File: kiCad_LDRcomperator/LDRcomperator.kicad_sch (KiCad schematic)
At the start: 9 parts, among them J1 Screw_Terminal_01x02

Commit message: updated the LDRComperator kicad drawing
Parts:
- removed Output1: Conn_01x01_MountingPin, Connector_PinSocket_2.54mm:PinSocket_1x01_P2.54mm_Vertical, symbol Connector_Generic_MountingPin:Conn_01x01_MountingPin
- added J2, J3: Conn_01x02_MountingPin, Connector_PinSocket_2.54mm:PinSocket_1x02_P2.54mm_Vertical, symbol Connector_Generic_MountingPin:Conn_01x02_MountingPin
- added LED2: LED, LED_THT:LED_D1.8mm_W3.3mm_H2.4mm, symbol Device:LED
- added R5: 65 ohm, Resistor_THT:R_Axial_DIN0204_L3.6mm_D1.6mm_P7.62mm_Horizontal, symbol Device:R
- added R6: LDR03, TerminalBlock_Phoenix:TerminalBlock_Phoenix_MKDS-1,5-2_1x02_P5.00mm_Horizontal, symbol Sensor_Optical:LDR03
- added R7: 2,2k ohm, Resistor_THT:R_Axial_DIN0204_L3.6mm_D1.6mm_P7.62mm_Horizontal, symbol Device:R
- J1, R2: footprint Connector_PinSocket_2.54mm:PinSocket_1x02_P2.54mm_Vertical -> TerminalBlock_Phoenix:TerminalBlock_Phoenix_MKDS-1,5-2_1x02_P5.00mm_Horizontal
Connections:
- net +3V3: now also R6.1
- net GND: now also LED2.1 (K), R7.2
- net at Op-amp1.1, R4.1: now also J2.1 (Pin_1), J2.2 (Pin_2)
- net at Op-amp1.3 (+), Potentiometer1.2, R1.2: now also Op-amp1.5 (+)
- new net: LED2.2 (A), R5.2
- new net: Op-amp1.6 (-), R6.2, R7.1
- new net: J3.1 (Pin_1), J3.2 (Pin_2), Op-amp1.7, R5.1
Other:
- moved on the sheet: J1, LED1, Potentiometer1, R1, R2, R3, R4

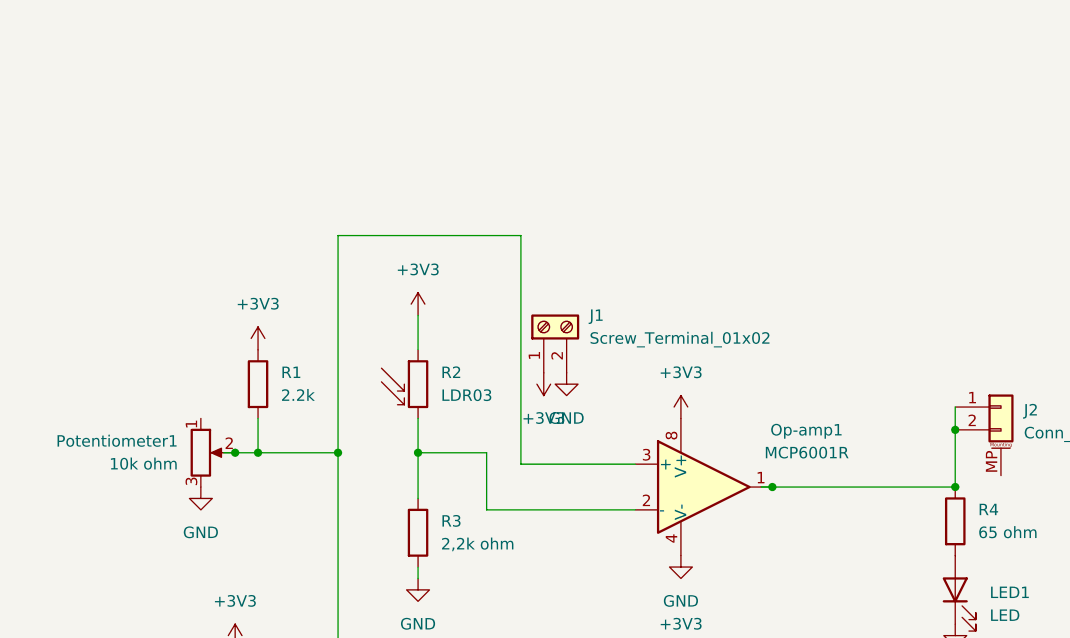
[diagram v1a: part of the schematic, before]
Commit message: kicad improvments for ldrCompartor
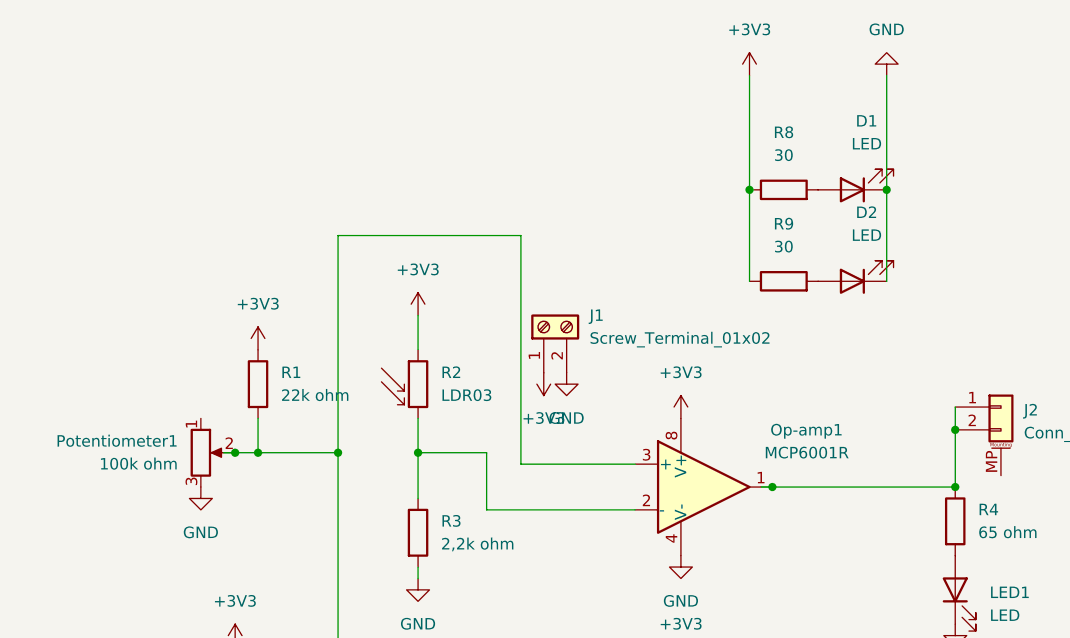
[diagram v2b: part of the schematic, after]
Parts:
- added D1, D2: LED, TerminalBlock_Phoenix:TerminalBlock_Phoenix_MKDS-1,5-2_1x02_P5.00mm_Horizontal, symbol Device:LED
- added R8, R9: 30, Resistor_THT:R_Axial_DIN0204_L3.6mm_D1.6mm_P7.62mm_Horizontal, symbol Device:R
- Potentiometer1: value 10k ohm -> 100k ohm
- R1: value 2.2k -> 22k ohm
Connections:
- net +3V3: now also R8.1, R9.1
- net GND: now also D1.1 (K), D2.1 (K)
- new net: D1.2 (A), R8.2
- new net: D2.2 (A), R9.2

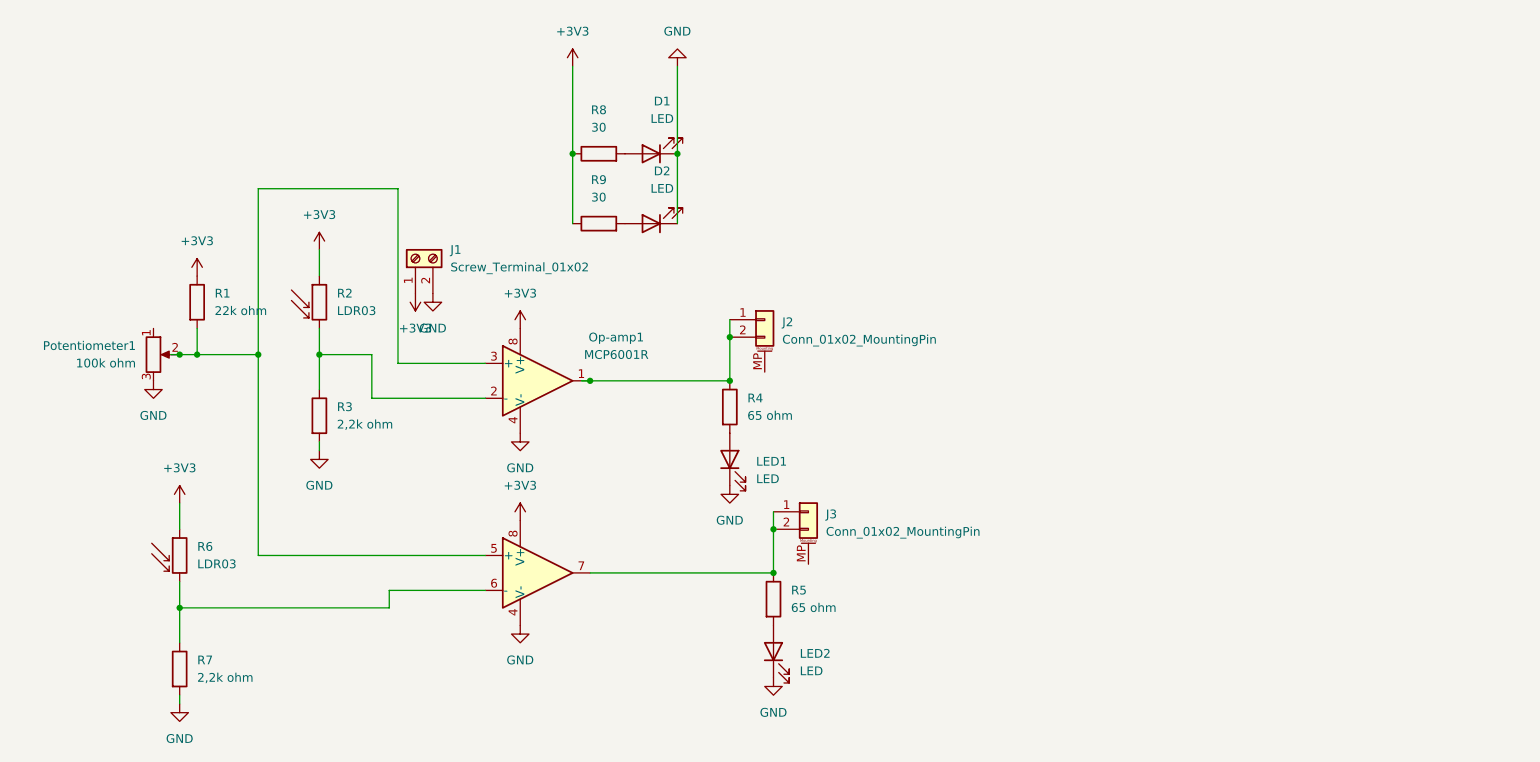
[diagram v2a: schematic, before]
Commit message: made flip flop work
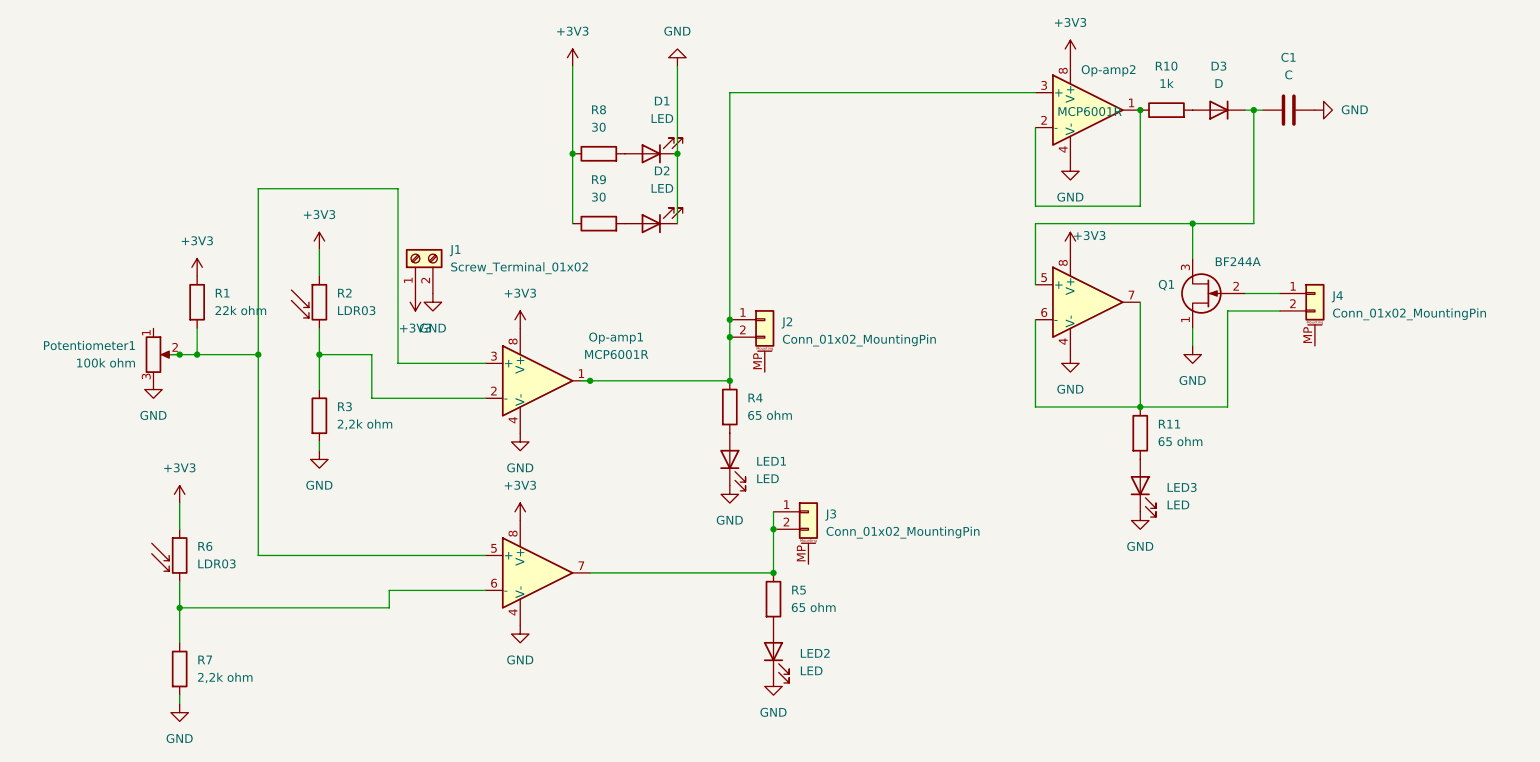
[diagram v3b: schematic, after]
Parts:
- added C1: C, symbol Device:C
- added D3: D, symbol Device:D
- added J4: Conn_01x02_MountingPin, Connector_PinSocket_2.54mm:PinSocket_1x02_P2.54mm_Vertical, symbol Connector_Generic_MountingPin:Conn_01x02_MountingPin
- added LED3: LED, LED_THT:LED_D1.8mm_W3.3mm_H2.4mm, symbol Device:LED
- added Op-amp2: MCP6001R, Package_DIP:DIP-8_W7.62mm, symbol Amplifier_Operational:MCP6001R
- added Q1: BF244A, Package_TO_SOT_THT:TO-92_Inline, symbol Transistor_FET:BF244A
- added R10: 1k, Resistor_THT:R_Axial_DIN0204_L3.6mm_D1.6mm_P7.62mm_Horizontal, symbol Device:R
- added R11: 65 ohm, Resistor_THT:R_Axial_DIN0204_L3.6mm_D1.6mm_P7.62mm_Horizontal, symbol Device:R
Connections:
- net +3V3: now also Op-amp2.8 (V+)
- net GND: now also C1.2, LED3.1 (K), Op-amp2.4 (V-), Q1.1 (D)
- net at J2.1 (Pin_1), J2.2 (Pin_2), Op-amp1.1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: now also Op-amp2.3 (+)
- new net: J4.2 (Pin_2), Op-amp2.6 (-), Op-amp2.7, R11.1
- new net: LED3.2 (A), R11.2
- new net: C1.1, D3.1 (K), Op-amp2.5 (+), Q1.3 (S)
- new net: D3.2 (A), R10.2
- new net: Op-amp2.1, Op-amp2.2 (-), R10.1
- new net: J4.1 (Pin_1), Q1.2 (G)
